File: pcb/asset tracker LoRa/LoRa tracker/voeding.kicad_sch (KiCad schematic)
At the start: 8 parts, among them J1 Screw_Terminal_01x02, U1 INA219BxDCN, U2 R-783.3-1.0

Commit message: klaar
print hertekend naar stm32L5
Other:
- note added: "slave adderes = 0x40"
- moved on the sheet: C1, C2, C3, C4

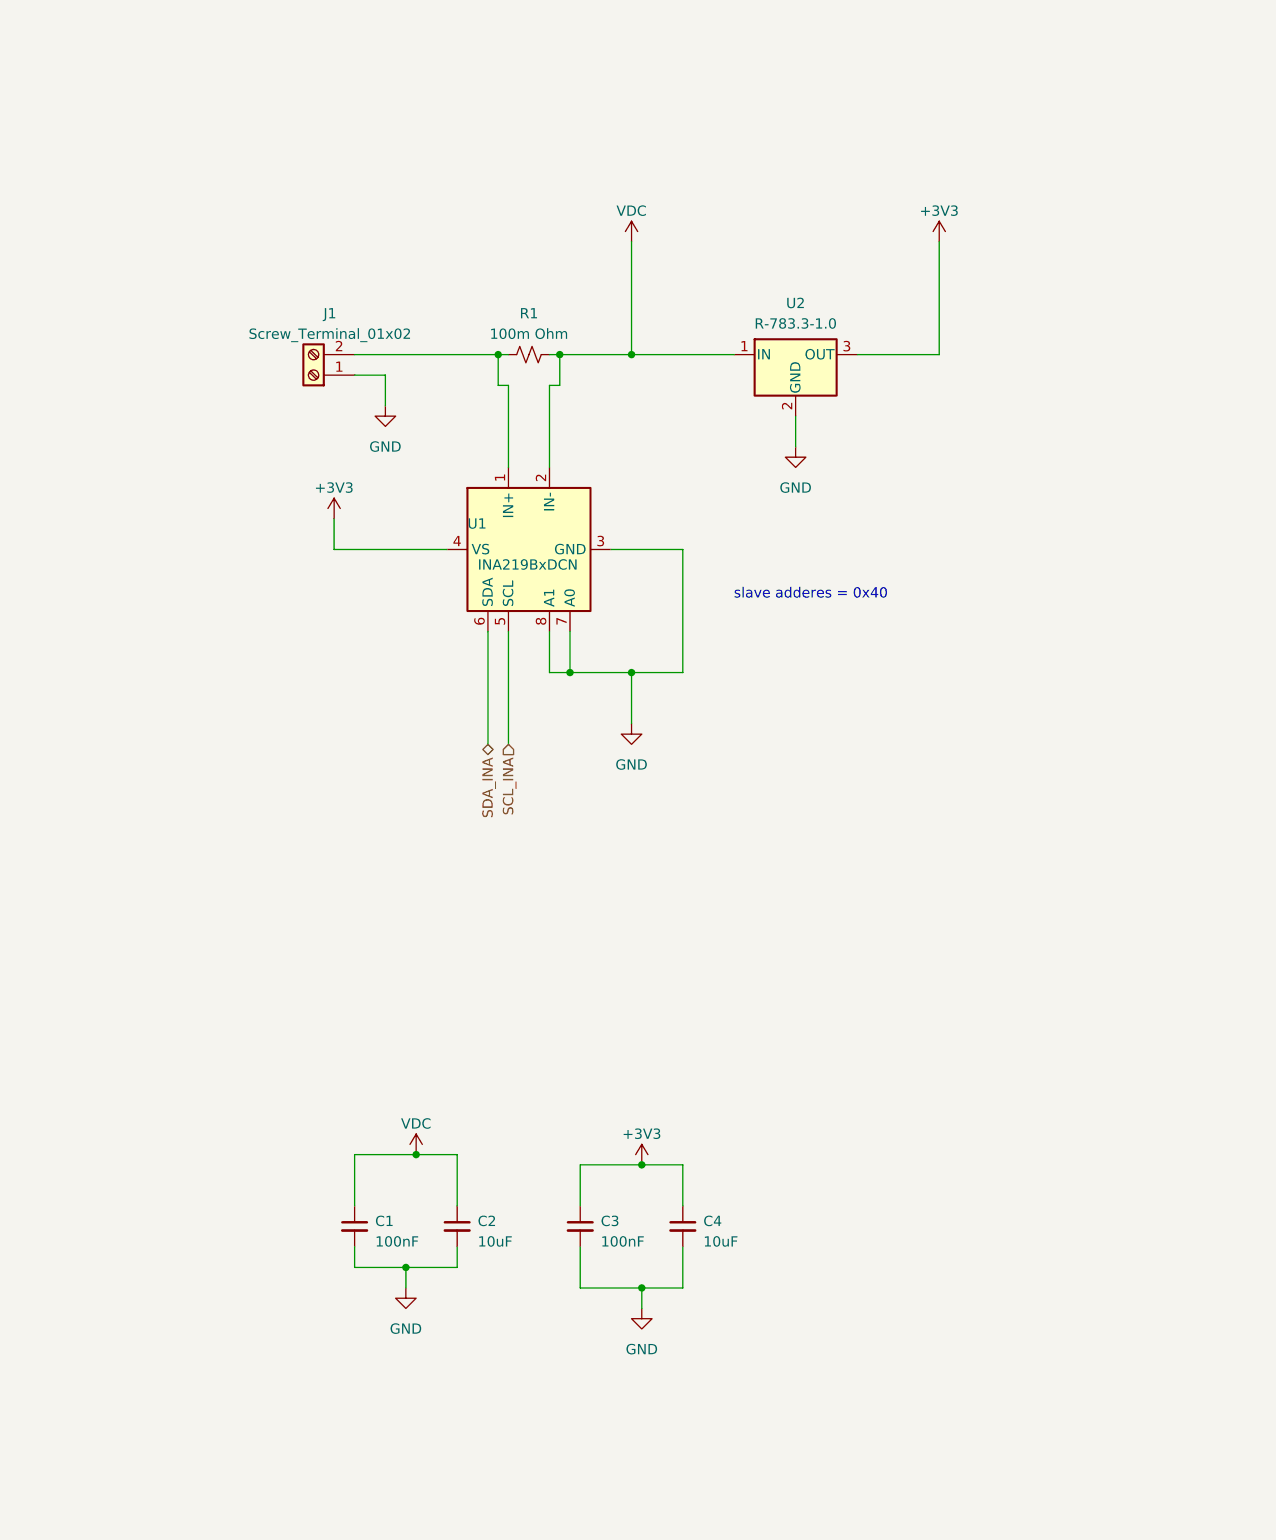
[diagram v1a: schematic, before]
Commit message: versie2
aan versie 2 begonnen met tekenen en code beginnen schrijven voor quadkey
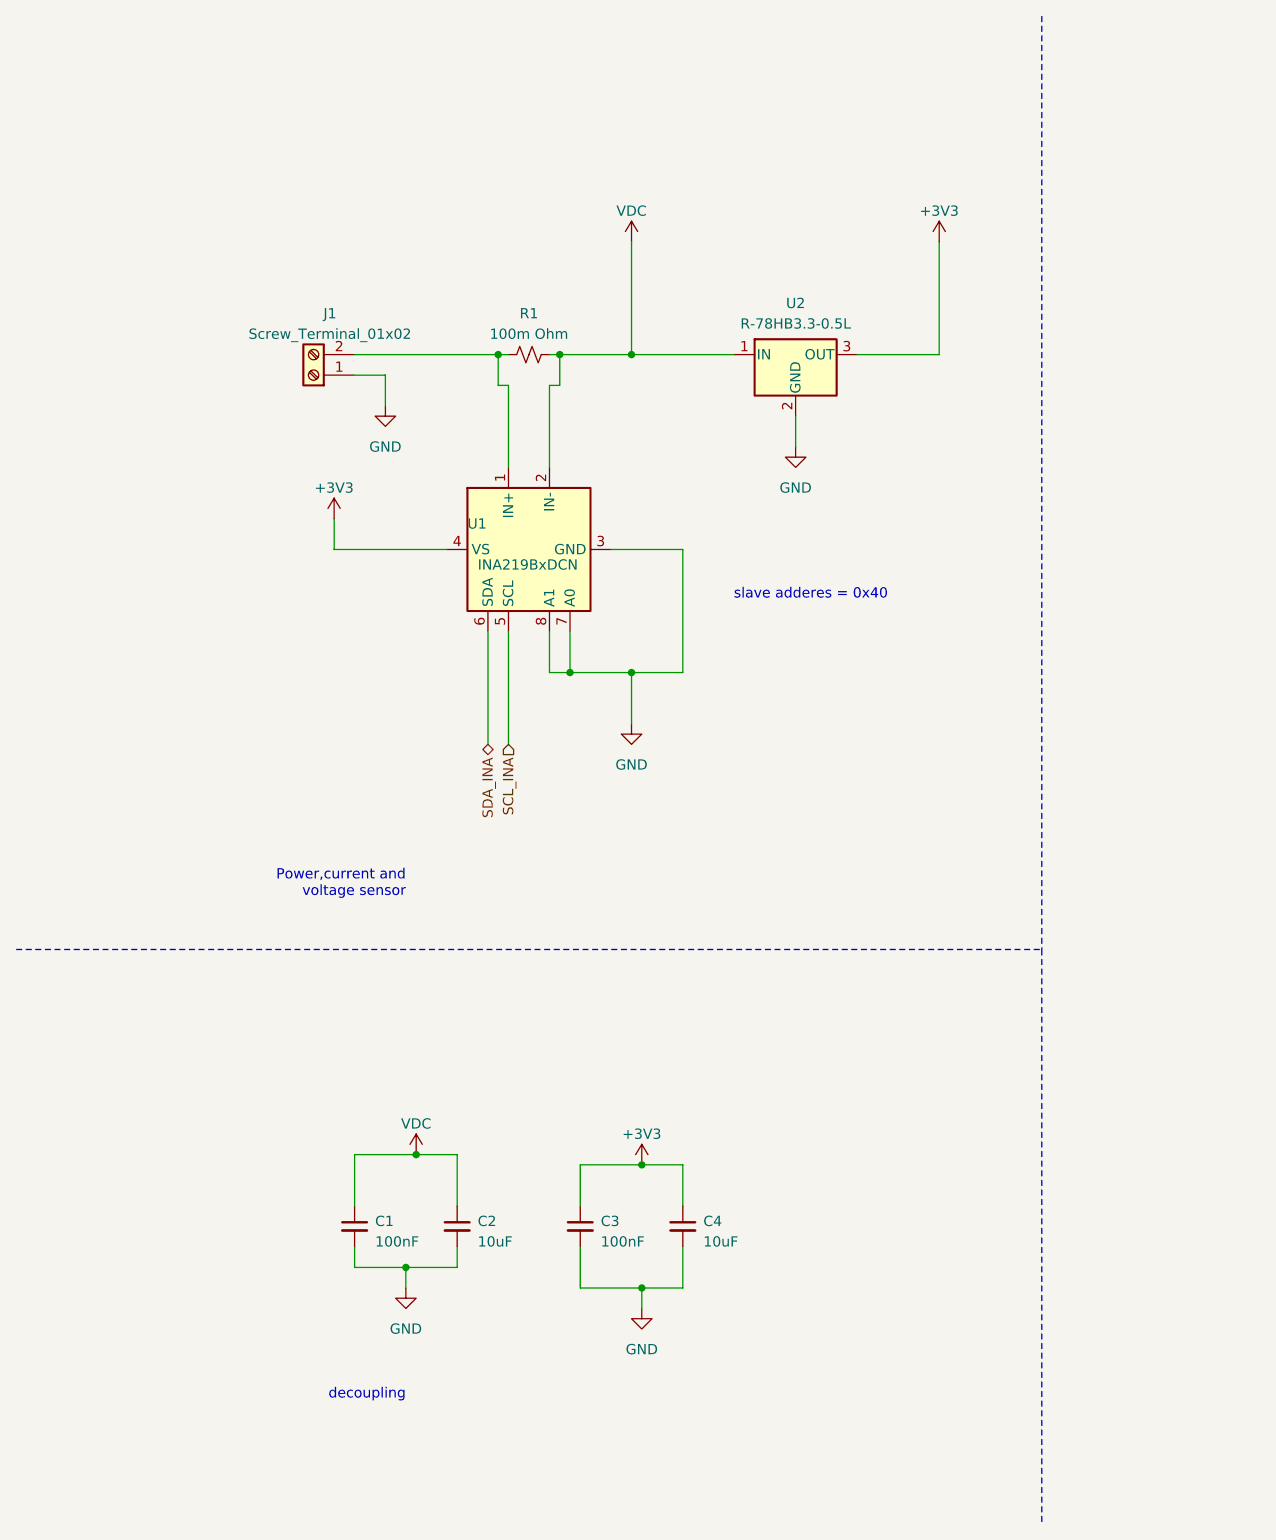
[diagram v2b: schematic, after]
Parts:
- U2: value R-783.3-1.0 -> R-78HB3.3-0.5L
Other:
- note added: "Power,current and voltage sensor"
- note added: "decoupling"
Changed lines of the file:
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@@
     (stroke (width 0) (type solid) (color 0 0 0 0))
+  )
+  (polyline (pts (xy 12.7 127) (xy 139.7 127))
+    (stroke (width 0) (type dash) (color 0 0 0 0))
+  )
+  (polyline (pts (xy 139.7 11.43) (xy 139.7 127))
+    (stroke (width 0) (type dash) (color 0 0 0 0))
+  )
+  (polyline (pts (xy 139.7 127) (xy 139.7 198.12))
+    (stroke (width 0) (type dash) (color 0 0 0 0))
+  )
+  (text "Power,current and \nvoltage sensor" (at 60.96 120.65 180)
+    (effects (font (size 1.27 1.27)) (justify right bottom))
+  )
+  (text "decoupling" (at 60.96 182.88 180)
+    (effects (font (size 1.27 1.27)) (justify right bottom))
   )
   (text "slave adderes = 0x40\n" (at 120.65 83.82 180)
@@
     (in_bom yes) (on_board yes) (fields_autoplaced)
     (property "Reference" "U2" (id 0) (at 109.22 46.99 0))
-    (property "Value" "R-783.3-1.0" (id 1) (at 109.22 49.53 0))
+    (property "Value" "R-78HB3.3-0.5L" (id 1) (at 109.22 49.53 0))
     (property "Footprint" "vanalles:recom psu" (id 2) (at 110.49 59.69 0)
       (effects (font (size 1.27 1.27) italic) (justify left) hide)
